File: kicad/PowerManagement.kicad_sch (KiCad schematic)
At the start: 30 parts, among them U13 AMS1117-3.3, U3 MP9488GS-Z, U5 AP63205

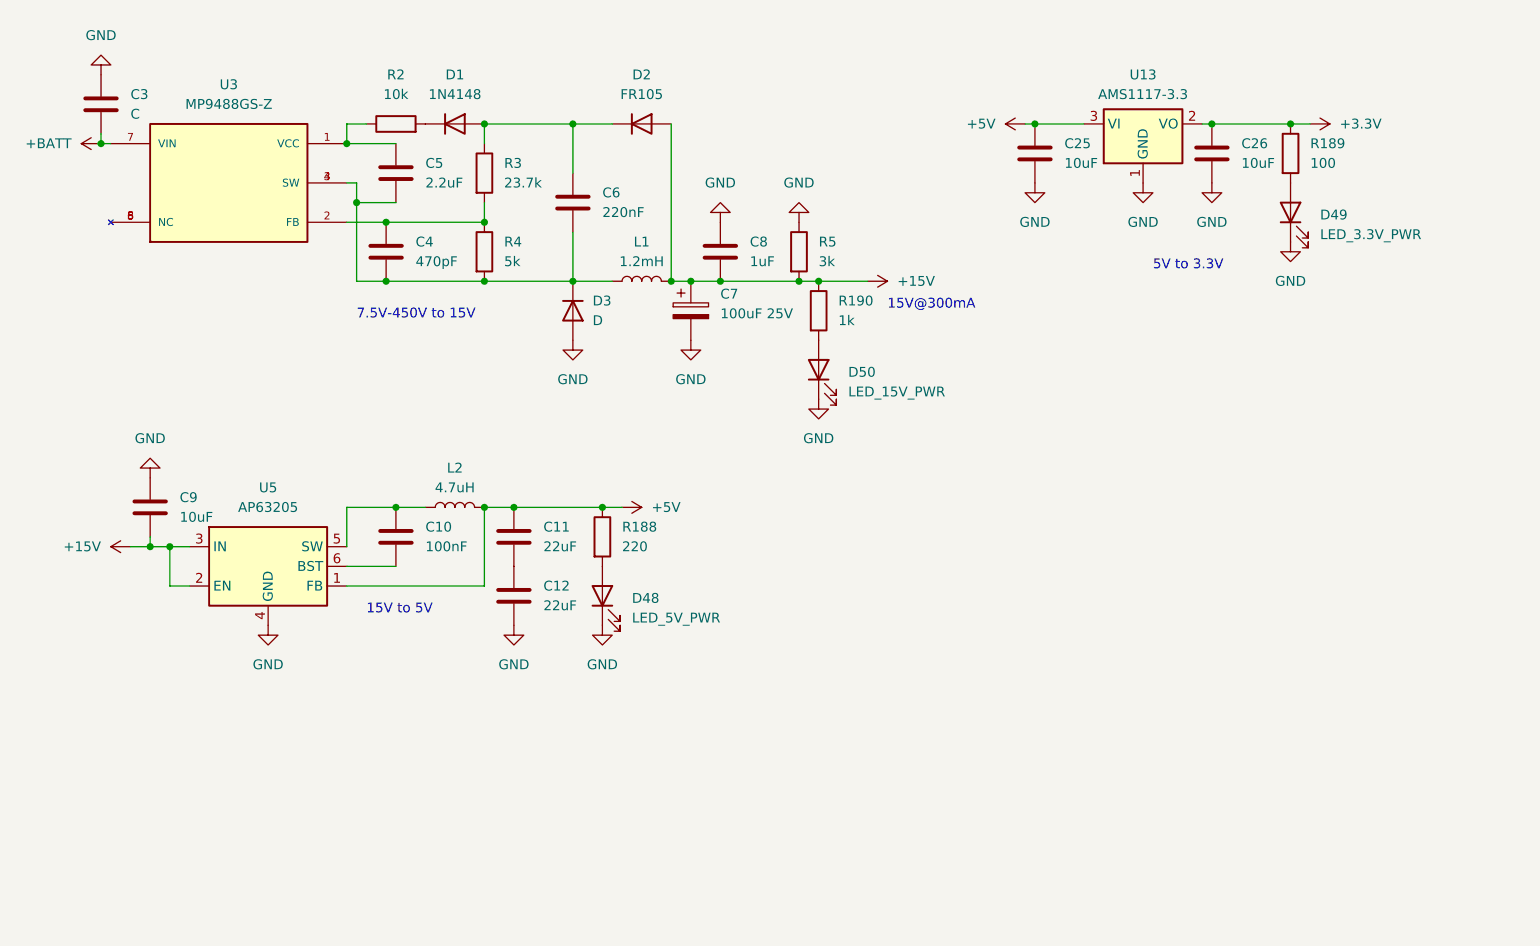
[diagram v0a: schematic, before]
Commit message: Replaced Rust with a CubeMX-generated C++ project.\nYes, sadly, Rust is pretty bad on embedded compared to C++
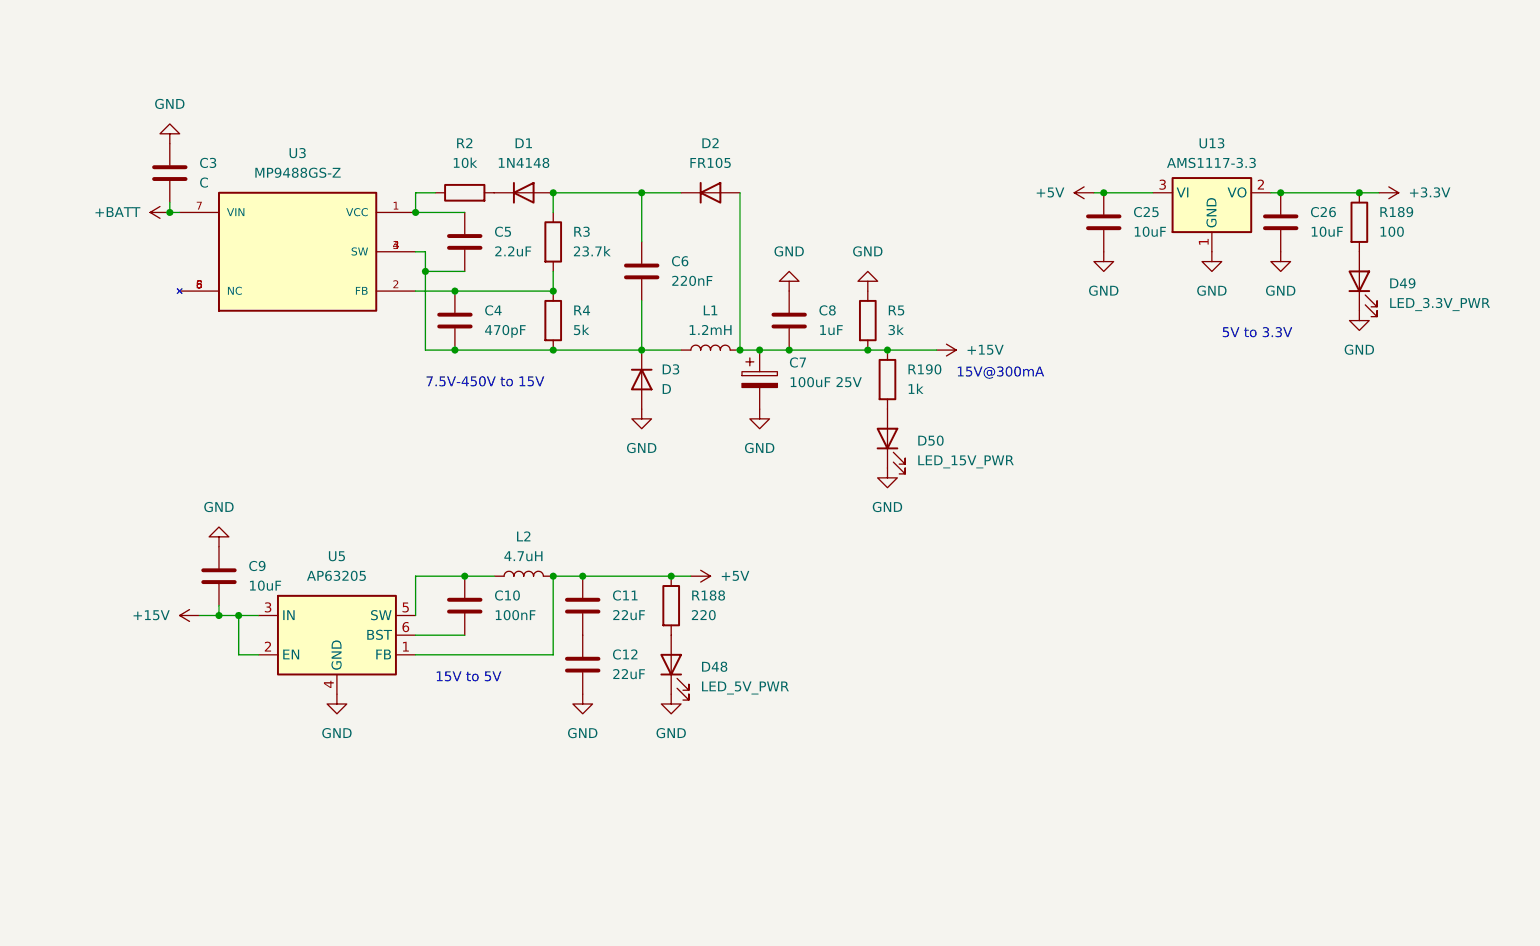
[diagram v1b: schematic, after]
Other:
- title: Power management -> Power sources
- moved on the sheet: C10, C11, C12, C25, C26, C3, C4, C5, C6, C7, C8, C9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

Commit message: Added charge MOSFET
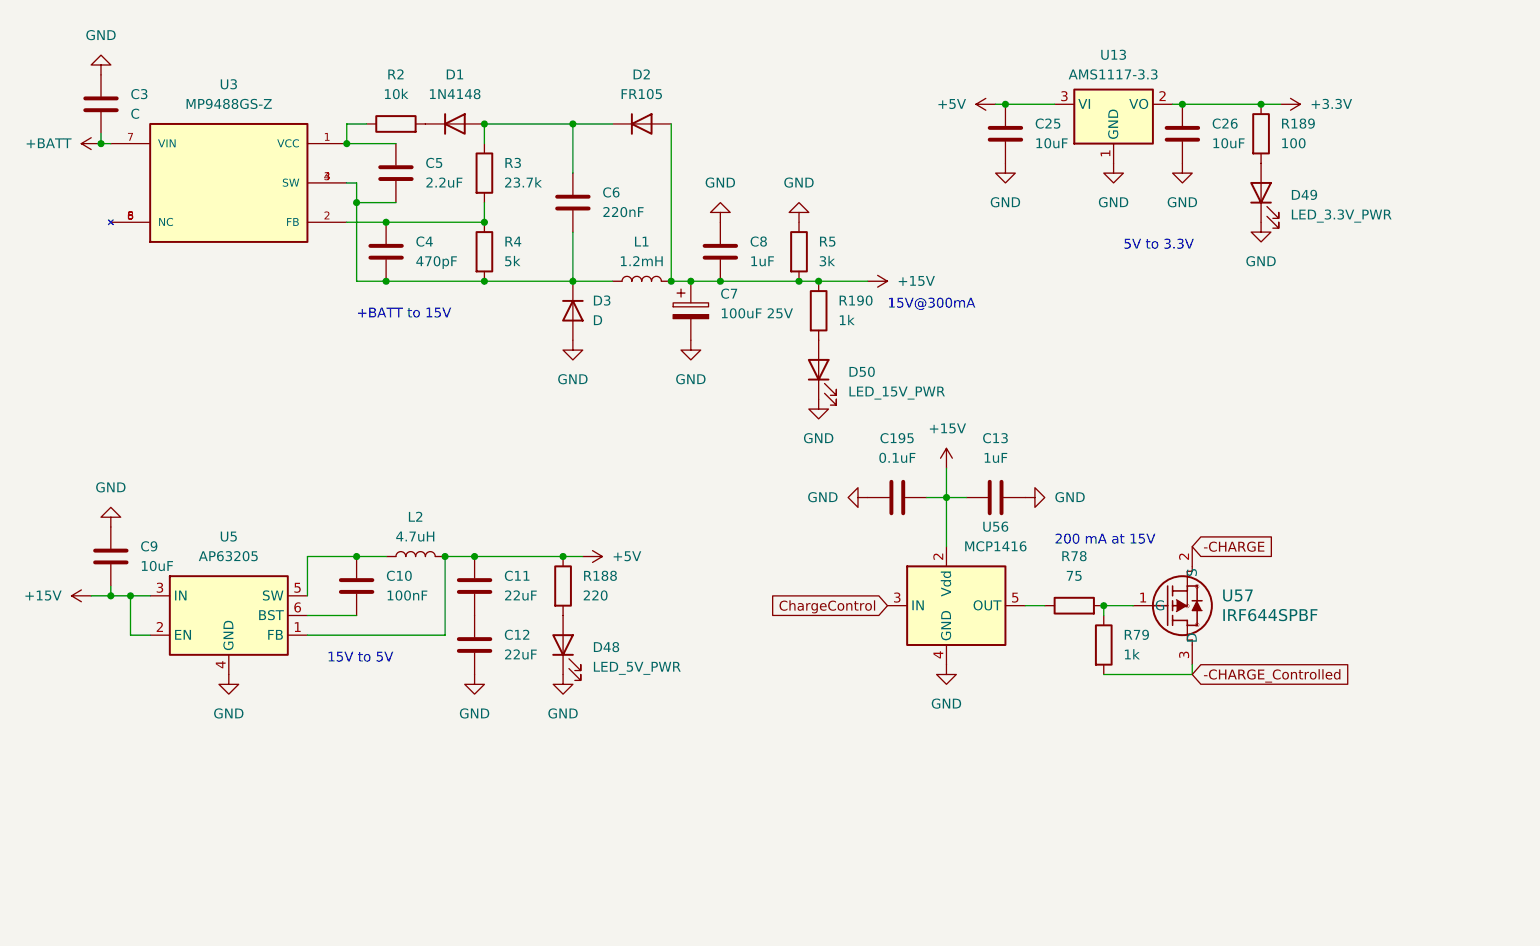
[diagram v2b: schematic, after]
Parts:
- added C13: 1uF, symbol Device:C
- added C195: 0.1uF, symbol Device:C
- added R78: 75, symbol Device:R
- added R79: 1k, symbol Device:R
- added U56: MCP1416, Package_TO_SOT_SMD:SOT-23-5, symbol Driver_FET:MCP1416
- added U57: IRF644SPBF, D2PAK_VIS, symbol IRF644SPBF:IRF644SPBF
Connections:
- net +15V: now also C13.1, C195.2, U56.2 (Vdd)
- net GND: now also C13.2, C195.1, U56.4 (GND)
- new net: R78.1, U56.5 (OUT)
- new net: R78.2, R79.1, U57.1 (G)
- new net -CHARGE: U57.2 (S)
- new net -CHARGE_Controlled: R79.2, U57.3 (D)
- new net ChargeControl: U56.3 (IN)
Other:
- note added: "+BATT to 15V"
- note added: "200 mA at 15V"
- note removed: "7.5V-450V to 15V"
- moved on the sheet: C10, C11, C12, C25, C26, C3, C4, C5, C6, C7, C8, C9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

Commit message: Added eFuses for 5V and 3.3V power rails
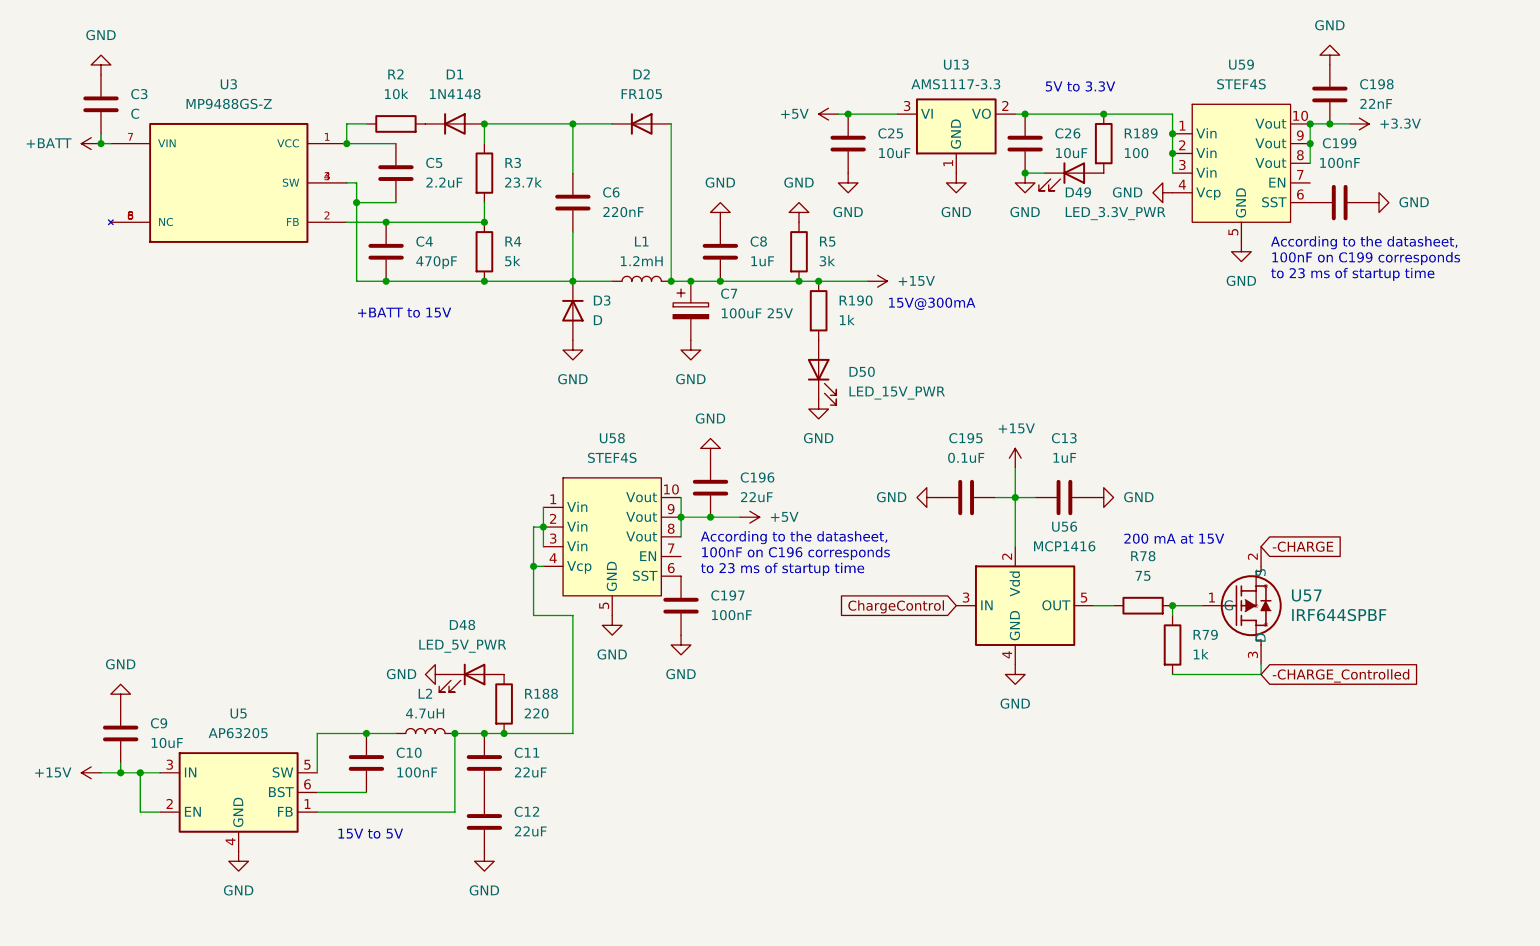
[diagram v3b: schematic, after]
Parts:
- added C196: 22uF, symbol Device:C
- added C197, C199: 100nF, symbol Device:C
- added C198: 22nF, symbol Device:C
- added U58, U59: STEF4S, Package_DFN_QFN:DFN-10-1EP_3x3mm_P0.5mm_EP1.55x2.48mm, symbol Power_Protection:STEF4S
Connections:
- net +3.3V: now also C198.1, U59.10 (Vout), U59.8 (Vout), U59.9 (Vout); no longer C26.1, R189.1, U13.2 (VO)
- net +5V: now also C196.2, U58.10 (Vout), U58.8 (Vout), U58.9 (Vout); no longer C11.1, L2.2, R188.1, U5.1 (FB)
- net GND: now also C196.1, C197.1, C198.2, C199.1, U58.5 (GND), U59.4 (Vcp), U59.5 (GND)
- net at R188.2: now also C11.1, L2.2, U5.1 (FB), U58.1 (Vin), U58.2 (Vin), U58.3 (Vin), U58.4 (Vcp); no longer D48.2 (A)
- new net: D48.2 (A), R188.1
- new net: C199.2, U59.6 (SST)
- new net: C26.1, R189.1, U13.2 (VO), U59.1 (Vin), U59.2 (Vin), U59.3 (Vin)
- new net: C197.2, U58.6 (SST)
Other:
- note added: "According to the datasheet, 100nF on C196 corresponds to 23 ms of startup time"
- note added: "According to the datasheet, 100nF on C199 corresponds to 23 ms of startup time"
- moved on the sheet: C10, C11, C12, C13, C195, C25, C26, C9, D48, D49, L2, R188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

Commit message: Started adding better temp sensors (SBMS-T-1)
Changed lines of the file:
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@@
   )
   (text "According to the datasheet,\n100nF on C199 corresponds\nto 23 ms of startup time"
-    (at 176.53 46.99 0)
-    (effects (font (size 1.27 1.27)) (justify left bottom))
+    (at 196.85 54.61 0)
+    (effects (font (size 1.27 1.27)) (justify right bottom))
   )
   (text "15V@300mA\n" (at 127 50.8 0)

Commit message: Small refactors
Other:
- note added: "According to the STEP4S datasheet, 100nF on C196/C199 corresponds to 23 ms of startup time"
- note removed: "According to the datasheet, 100nF on C196 corresponds to 23 ms of startup time"
- note removed: "According to the datasheet, 100nF on C199 corresponds to 23 ms of startup time"
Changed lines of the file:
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@@
     (effects (font (size 1.27 1.27)) (justify left bottom))
-  )
-  (text "According to the datasheet,\n100nF on C199 corresponds\nto 23 ms of startup time"
-    (at 196.85 54.61 0)
-    (effects (font (size 1.27 1.27)) (justify right bottom))
   )
   (text "15V@300mA\n" (at 127 50.8 0)
@@
     (effects (font (size 1.27 1.27)) (justify left bottom))
   )
-  (text "According to the datasheet,\n100nF on C196 corresponds\nto 23 ms of startup time"
-    (at 102.87 85.09 0)
+  (text "According to the STEP4S datasheet,\n100nF on C196/C199 corresponds\nto 23 ms of startup time"
+    (at 38.1 74.93 0)
     (effects (font (size 1.27 1.27)) (justify left bottom))
   )

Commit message: Finished SBMS-T-3, started work on SBMS-T-4
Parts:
- removed C3: C, symbol Device:C
- removed C4: 470pF, symbol Device:C
- removed C5: 2.2uF, symbol Device:C
- removed C6: 220nF, symbol Device:C
- removed C7: 100uF 25V, symbol Device:C_Polarized
- removed C8: 1uF, symbol Device:C
- removed D1: 1N4148, symbol Device:D
- removed D2: FR105, symbol Device:D
- removed D3: D, symbol Device:D
- removed L1: 1.2mH, symbol Device:L
- removed R2: 10k, symbol Device:R
- removed R3: 23.7k, symbol Device:R
- removed R4: 5k, symbol Device:R
- removed R5: 3k, symbol Device:R
- removed U3: MP9488GS-Z, MP9488GS-Z:SOIC127P600X175-8N, symbol MP9488GS-Z:MP9488GS-Z
- D50: value LED_15V_PWR -> LED_4S_PWR
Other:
- note removed: "+BATT to 15V"
- note removed: "15V@300mA"
- moved on the sheet: C10, C11, C12, C13, C195, C196, C197, C198, C199, C25, C26, C9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

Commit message: fixed typo in ports
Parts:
- U57: footprint D2PAK_VIS -> D2PAK_VIS:D2PAK_VIS
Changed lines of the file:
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@@
       (effects (font (size 1.524 1.524)) (justify left))
     )
-    (property "Footprint" "D2PAK_VIS" (at 162.56 83.82 0)
+    (property "Footprint" "D2PAK_VIS:D2PAK_VIS" (at 162.56 83.82 0)
       (effects (font (size 1.27 1.27) italic) hide)
     )
